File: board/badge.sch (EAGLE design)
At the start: 43 parts, among them IC1 STM32F030F4, IC2 UBLOX_MAX, IC3 RFM69HW, IC4 MCP1640, J2 20-0096, J3 SWD_PTH_SHROUD, X1 RADIOMETRIX-MTX2, X2 SMA-142-0701-851/861, X3 091OLED

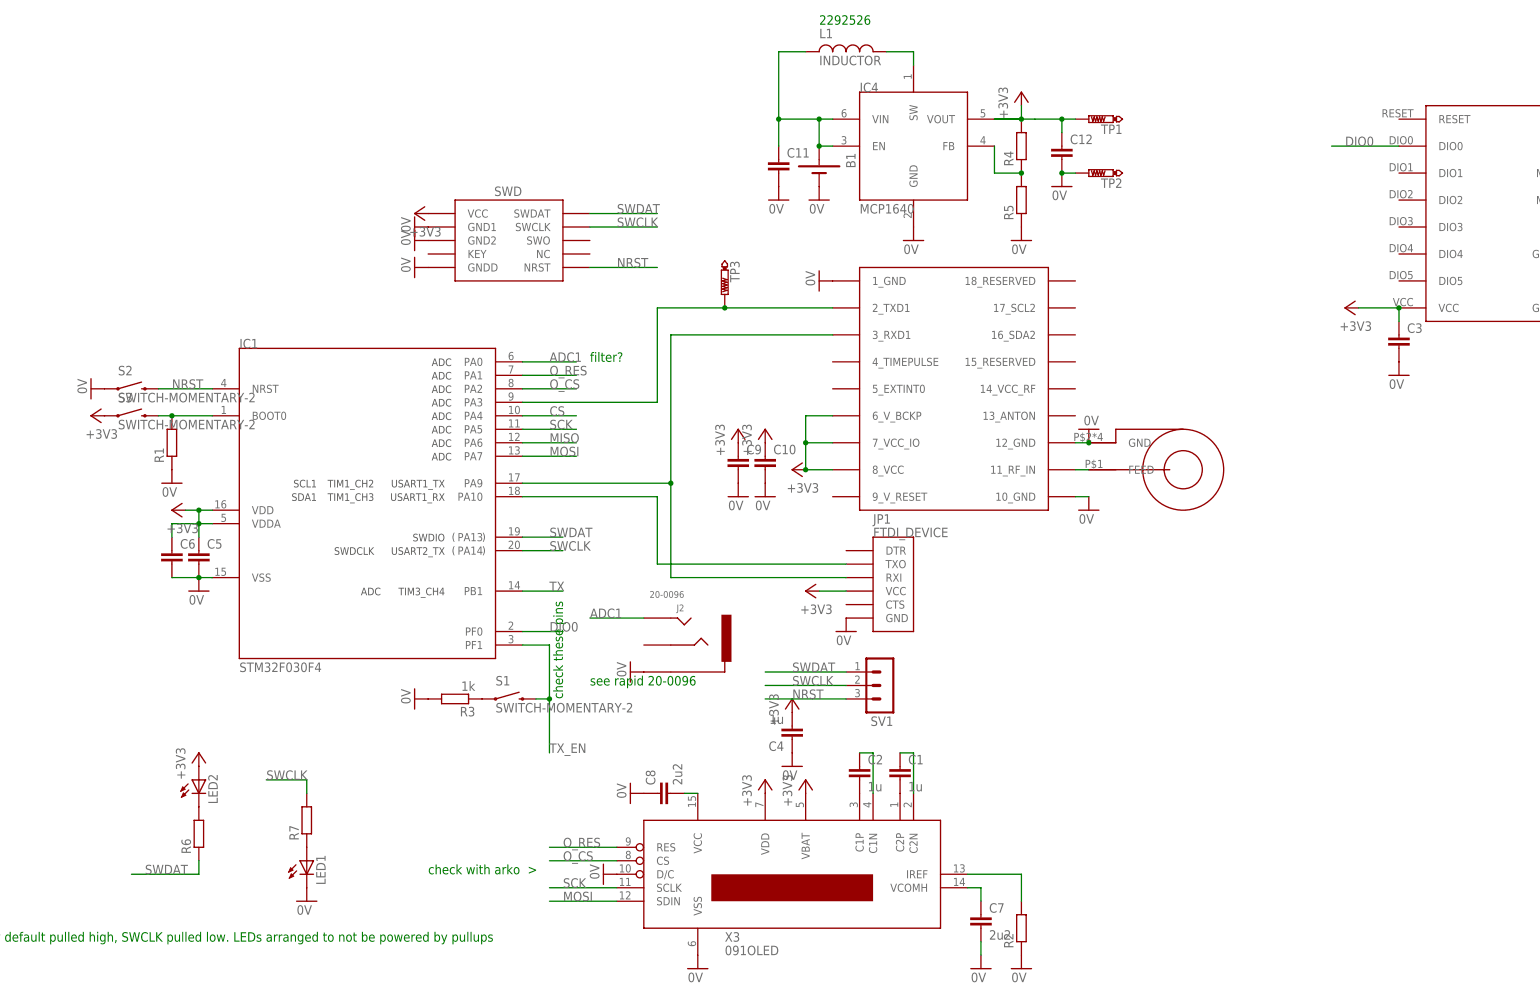
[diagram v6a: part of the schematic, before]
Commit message: adding part numbers
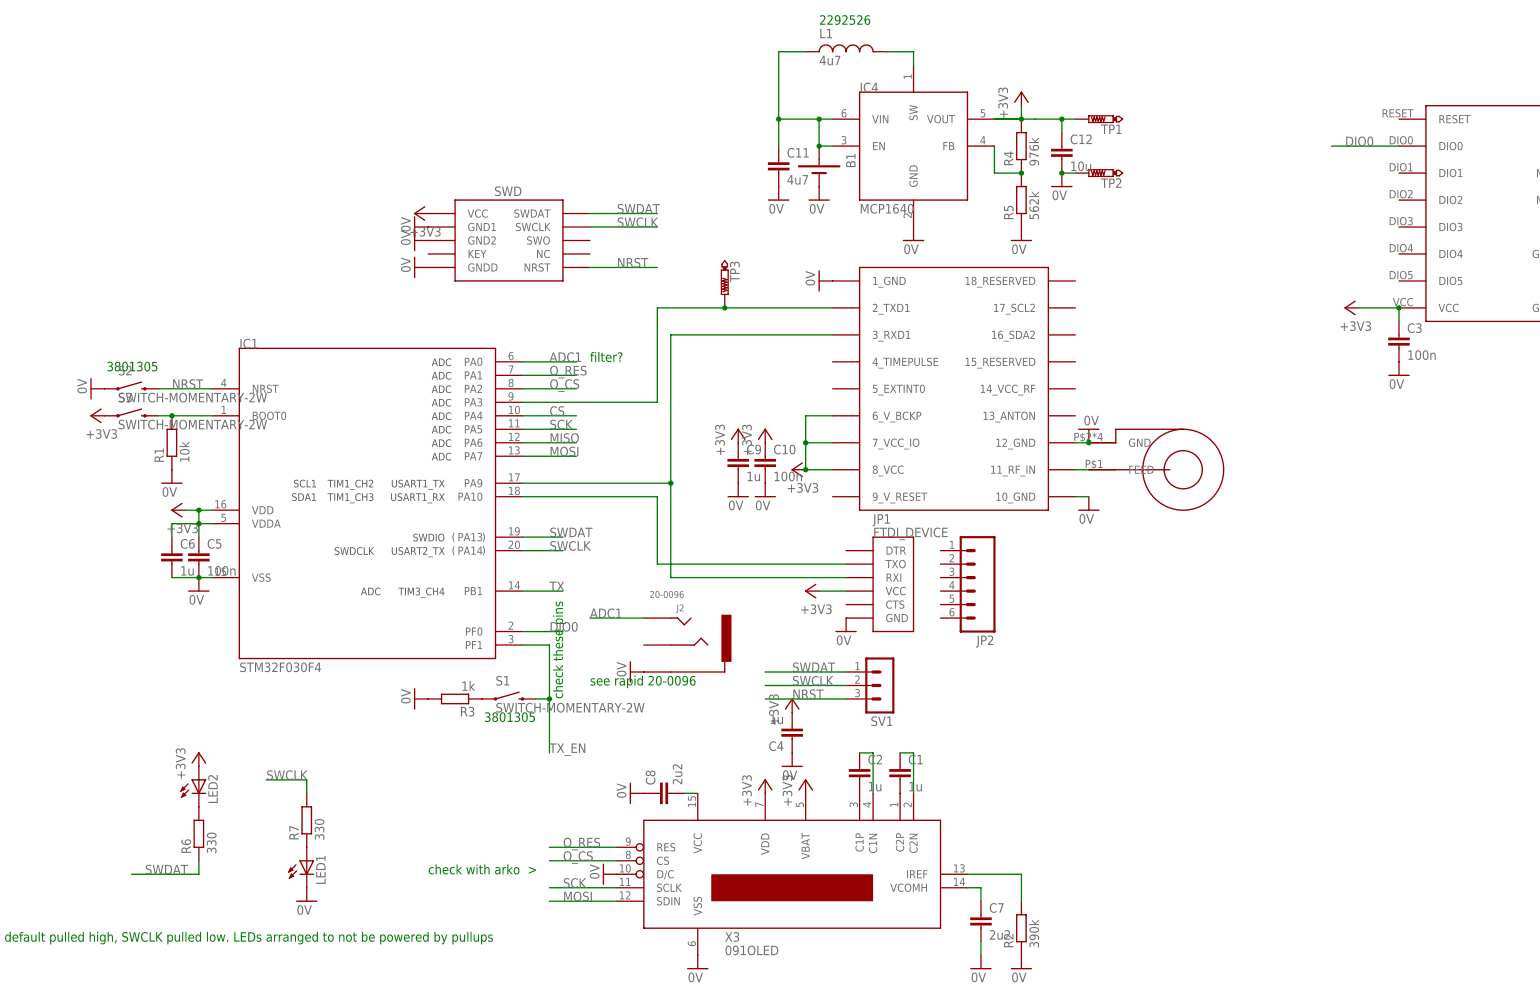
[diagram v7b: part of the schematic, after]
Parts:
- added JP2: (no value), SparkFun-Connectors:M06SMD
- C10, C3, C5: value (none) -> 100n
- C11: value (none) -> 4u7
- C12: value (none) -> 10u
- C6, C9: value (none) -> 1u
- L1: value INDUCTOR -> 4u7
- R1: value (none) -> 10k
- R2: value (none) -> 390k
- R4: value (none) -> 976k
- R5: value (none) -> 562k
- R6, R7: value (none) -> 330
- S1, S2, S3: value SWITCH-MOMENTARY-2 -> SWITCH-MOMENTARY-2W; device SparkFun-Electromechanical:SWITCH-MOMENTARY-2 -> ukhas:SWITCH-MOMENTARY-2W
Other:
- note added: "3801305"
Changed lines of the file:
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@@
 <part name="IC4" library="ukhas" deviceset="MCP1640" device=""/>
 <part name="JP1" library="SparkFun-Connectors" deviceset="FTDI_DEVICE" device=""/>
-<part name="S2" library="SparkFun-Electromechanical" deviceset="SWITCH-MOMENTARY-2" device=""/>
-<part name="S3" library="SparkFun-Electromechanical" deviceset="SWITCH-MOMENTARY-2" device=""/>
+<part name="S2" library="ukhas" deviceset="SWITCH-MOMENTARY-2" device="W"/>
+<part name="S3" library="ukhas" deviceset="SWITCH-MOMENTARY-2" device="W"/>
 <part name="J3" library="dtb" deviceset="SWD_PTH_SHROUD" device=""/>
 <part name="+3V1" library="supply1" deviceset="+3V3" device=""/>
@@
 <part name="GND8" library="supply1" deviceset="0V" device=""/>
 <part name="GND9" library="supply1" deviceset="0V" device=""/>
-<part name="C5" library="rcl" deviceset="C-EU" device="C0603"/>
-<part name="C6" library="rcl" deviceset="C-EU" device="C0603"/>
-<part name="C10" library="rcl" deviceset="C-EU" device="C0603"/>
-<part name="C9" library="rcl" deviceset="C-EU" device="C0603"/>
+<part name="C5" library="rcl" deviceset="C-EU" device="C0603" value="100n"/>
+<part name="C6" library="rcl" deviceset="C-EU" device="C0603" value="1u"/>
+<part name="C10" library="rcl" deviceset="C-EU" device="C0603" value="100n"/>
+<part name="C9" library="rcl" deviceset="C-EU" device="C0603" value="1u"/>
 <part name="C2" library="rcl" deviceset="C-EU" device="C0603" value="1u"/>
 <part name="C1" library="rcl" deviceset="C-EU" device="C0603" value="1u"/>
@@
 <part name="GND10" library="supply1" deviceset="0V" device=""/>
 <part name="GND11" library="supply1" deviceset="0V" device=""/>
-<part name="R1" library="rcl" deviceset="R-EU_" device="R0603"/>
+<part name="R1" library="rcl" deviceset="R-EU_" device="R0603" value="10k"/>
 <part name="GND12" library="supply1" deviceset="0V" device=""/>
-<part name="R4" library="rcl" deviceset="R-EU_" device="R0603"/>
-<part name="R5" library="rcl" deviceset="R-EU_" device="R0603"/>
+<part name="R4" library="rcl" deviceset="R-EU_" device="R0603" value="976k"/>
+<part name="R5" library="rcl" deviceset="R-EU_" device="R0603" value="562k"/>
 <part name="GND13" library="supply1" deviceset="0V" device=""/>
 <part name="GND14" library="supply1" deviceset="0V" device=""/>
-<part name="C11" library="rcl" deviceset="C-EU" device="C0805"/>
-<part name="C12" library="rcl" deviceset="C-EU" device="C0805"/>
+<part name="C11" library="rcl" deviceset="C-EU" device="C0805" value="4u7"/>
+<part name="C12" library="rcl" deviceset="C-EU" device="C0805" value="10u"/>
 <part name="GND15" library="supply1" deviceset="0V" device=""/>
 <part name="GND16" library="supply1" deviceset="0V" device=""/>
-<part name="S1" library="SparkFun-Electromechanical" deviceset="SWITCH-MOMENTARY-2" device=""/>
-<part name="L1" library="ukhas" deviceset="INDUCTOR" device=""/>
+<part name="S1" library="ukhas" deviceset="SWITCH-MOMENTARY-2" device="W"/>
+<part name="L1" library="ukhas" deviceset="INDUCTOR" device="" value="4u7"/>
 <part name="GND17" library="supply1" deviceset="0V" device=""/>
 <part name="GND18" library="supply1" deviceset="0V" device=""/>
@@
 <part name="GND20" library="supply1" deviceset="0V" device=""/>
 <part name="+3V7" library="supply1" deviceset="+3V3" device=""/>
-<part name="C3" library="rcl" deviceset="C-EU" device="C0603"/>
+<part name="C3" library="rcl" deviceset="C-EU" device="C0603" value="100n"/>
 <part name="GND22" library="supply1" deviceset="0V" device=""/>
 <part name="+3V8" library="supply1" deviceset="+3V3" device=""/>
@@
 <part name="GND24" library="supply1" deviceset="0V" device=""/>
 <part name="C8" library="rcl" deviceset="C-EU" device="C0603" value="2u2"/>
-<part name="R2" library="rcl" deviceset="R-EU_" device="R0603"/>
+<part name="R2" library="rcl" deviceset="R-EU_" device="R0603" value="390k"/>
 <part name="GND25" library="supply1" deviceset="0V" device=""/>
 <part name="C7" library="rcl" deviceset="C-EU" device="C0603" value="2u2"/>
@@
 <part name="LED2" library="SparkFun-LED" deviceset="LED" device="0603"/>
 <part name="LED1" library="SparkFun-LED" deviceset="LED" device="0603"/>
-<part name="R6" library="rcl" deviceset="R-EU_" device="R0603"/>
-<part name="R7" library="rcl" deviceset="R-EU_" device="R0603"/>
+<part name="R6" library="rcl" deviceset="R-EU_" device="R0603" value="330"/>
+<part name="R7" library="rcl" deviceset="R-EU_" device="R0603" value="330"/>
 <part name="+3V13" library="supply1" deviceset="+3V3" device=""/>
 <part name="GND29" library="supply1" deviceset="0V" device=""/>
@@
 <part name="TP3" library="testpad" deviceset="PTR1" device="B2,54"/>
 <part name="J2" library="ukhas" deviceset="3.5MMJACKSMD" device="" value="20-0096"/>
+<part name="JP2" library="SparkFun-Connectors" deviceset="M06" device="SMD"/>
 </parts>
 <sheets>
@@
 <text x="2.54" y="106.68" size="1.778" layer="91">filter?</text>
 <text x="45.72" y="170.18" size="1.778" layer="91">2292526</text>
+<text x="-78.74" y="106.68" size="1.778" layer="91" rot="R180">3801305</text>
+<text x="-7.62" y="40.64" size="1.778" layer="91" rot="R180">3801305</text>
 </plain>
 <instances>
@@
 <instance part="TP3" gate="G$1" x="27.94" y="119.38" rot="R180"/>
 <instance part="J2" gate="G$1" x="22.86" y="53.34" rot="R180"/>
+<instance part="JP2" gate="G$1" x="73.66" y="66.04" rot="R180"/>
 </instances>
 <busses>

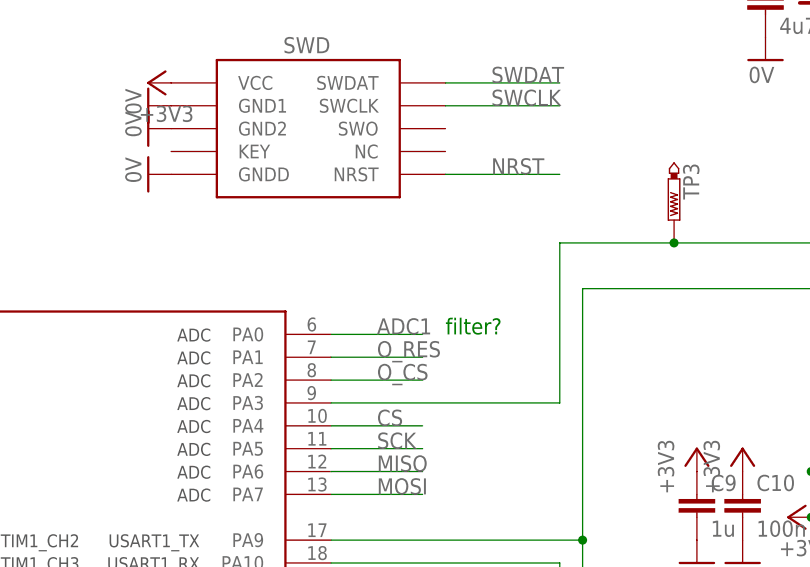
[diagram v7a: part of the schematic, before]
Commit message: adding DC bias resistors
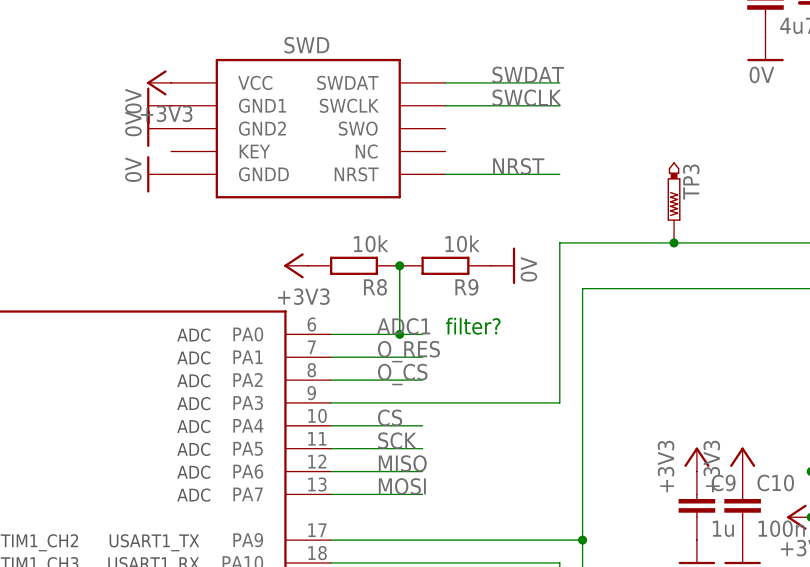
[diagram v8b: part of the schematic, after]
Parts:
- added R8, R9: 10k, rcl:R-EU_R0603
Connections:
- net +3V3: now also R8.2
- net 0V: now also R9.1
- net ADC1: now also R8.1, R9.2
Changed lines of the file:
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@@
 <part name="J2" library="ukhas" deviceset="3.5MMJACKSMD" device="" value="20-0096"/>
 <part name="JP2" library="SparkFun-Connectors" deviceset="M06" device="SMD"/>
+<part name="R8" library="rcl" deviceset="R-EU_" device="R0603" value="10k"/>
+<part name="R9" library="rcl" deviceset="R-EU_" device="R0603" value="10k"/>
+<part name="+3V17" library="supply1" deviceset="+3V3" device=""/>
+<part name="GND21" library="supply1" deviceset="0V" device=""/>
 </parts>
 <sheets>
@@
 <instance part="J2" gate="G$1" x="22.86" y="53.34" rot="R180"/>
 <instance part="JP2" gate="G$1" x="73.66" y="66.04" rot="R180"/>
+<instance part="R8" gate="G$1" x="-7.62" y="114.3" rot="R180"/>
+<instance part="R9" gate="G$1" x="2.54" y="114.3" rot="R180"/>
+<instance part="+3V17" gate="G$1" x="-15.24" y="114.3" rot="R90"/>
+<instance part="GND21" gate="1" x="10.16" y="114.3" rot="R90"/>
 </instances>
 <busses>
@@
 <wire x1="50.8" y1="63.5" x2="45.72" y2="63.5" width="0.1524" layer="91"/>
 </segment>
+<segment>
+<pinref part="R8" gate="G$1" pin="2"/>
+<pinref part="+3V17" gate="G$1" pin="+3V3"/>
+</segment>
 </net>
 <net name="0V" class="0">
@@
 <pinref part="J2" gate="G$1" pin="2"/>
 <pinref part="GND23" gate="1" pin="0V"/>
+</segment>
+<segment>
+<pinref part="R9" gate="G$1" pin="1"/>
+<pinref part="GND21" gate="1" pin="0V"/>
 </segment>
 </net>
@@
 <segment>
 <pinref part="IC1" gate="G$1" pin="PA0"/>
-<wire x1="-10.16" y1="106.68" x2="0" y2="106.68" width="0.1524" layer="91"/>
+<wire x1="-10.16" y1="106.68" x2="-2.54" y2="106.68" width="0.1524" layer="91"/>
 <label x="-5.08" y="106.68" size="1.778" layer="95"/>
-</segment>
-<segment>
+<pinref part="R8" gate="G$1" pin="1"/>
+<pinref part="R9" gate="G$1" pin="2"/>
+<wire x1="-2.54" y1="106.68" x2="0" y2="106.68" width="0.1524" layer="91"/>
+<wire x1="-2.54" y1="114.3" x2="-2.54" y2="106.68" width="0.1524" layer="91"/>
+<junction x="-2.54" y="106.68"/>
+<junction x="-2.54" y="114.3"/>
+</segment>
+<segment>
